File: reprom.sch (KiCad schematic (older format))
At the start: 20 parts, among them P1 KERNAL_SOCKET, P10 NEW_LEFT, P11 SX64_RIGHT, P12 ANCIENT_RIGHT, P13 GND, P2 KERNAL_AND_BASIC_SOCKET, P3 ANCIENT_LEFT, P4 OLD_RIGHT, P5 KERNAL, P6 CHARSET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

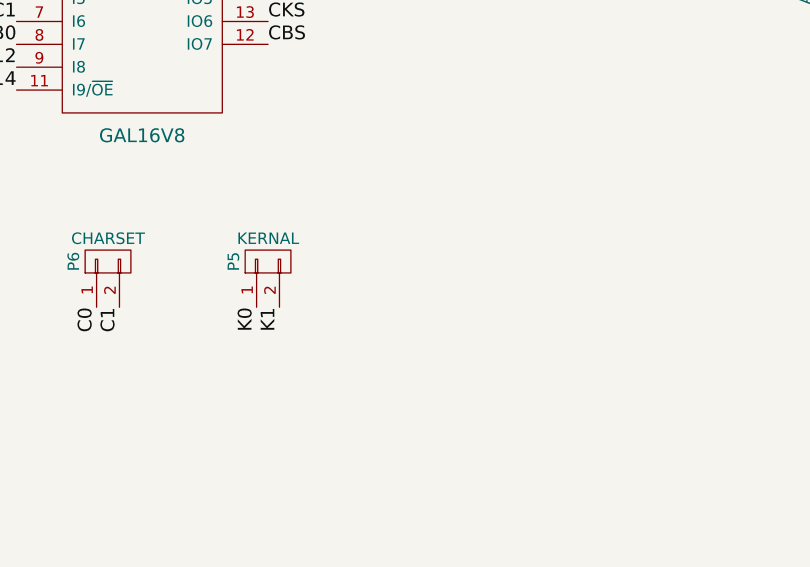
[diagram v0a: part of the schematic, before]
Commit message: Hardware: Added additional pin header for A5 and A8, rounded corners
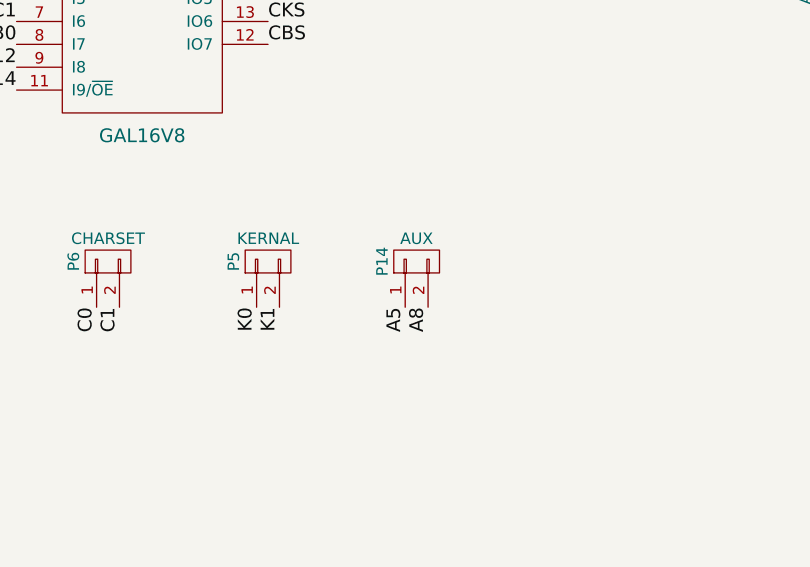
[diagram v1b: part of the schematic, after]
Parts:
- added P14: AUX, custom:Pin_Header_Straight_1x02, symbol CONN_01X02
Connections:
- net A5: now also P14.1 (P1)
- net A8: now also P14.2 (P2)
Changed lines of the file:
@@
 	1    0    0    -1
 $EndComp
+$Comp
+L CONN_01X02 P14
+U 1 1 57987F08
+P 9000 3700
+F 0 "P14" H 9000 3850 50  0000 C CNN
+F 1 "AUX" V 9100 3700 50  0000 C CNN
+F 2 "custom:Pin_Header_Straight_1x02" H 9000 3700 50  0001 C CNN
+F 3 "" H 9000 3700 50  0000 C CNN
+	1    9000 3700
+	0    -1   -1   0
+$EndComp
+Text Label 8950 3900 3    60   ~ 0
+A5
+Text Label 9050 3900 3    60   ~ 0
+A8
 $EndSCHEMATC
